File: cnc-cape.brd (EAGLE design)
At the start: 160.7 x 100.3 mm, 120 parts, among them IC1 LM2576hvt, IC2 74HC14N, IC3 74HC14N, IC4 74HCT244N, IC5 74HCT244N, IC6 74HC14N, IC7 LM1458N, J1 22-27-2041-04, J10 22-27-2031-03, J11 22-27-2031-03, J12 22-27-2031-03, J13 22-27-2031-03, J14 22-27-2031-03, J15 22-27-2031-03, J16 22-27-2031-03, J17 22-27-2031-03, J18 22-27-2031-03, J19 22-27-2031-03, J2 22-27-2041-04, J20 22-27-2031-03, J21 22-27-2031-03, J22 22-27-2031-03, J3 22-27-2041-04, J4 22-27-2041-04, J5 22-27-2041-04, J6 22-27-2031-03, J7 22-27-2031-03, J8 22-27-2031-03, J9 22-27-2031-03, K1 G2R2, K2 G2R2, K3 G2R2, Q1 2N7000, Q2 2N7000, T1 1n2222, T2 1n2222, T3 1n2222, X5 Power In

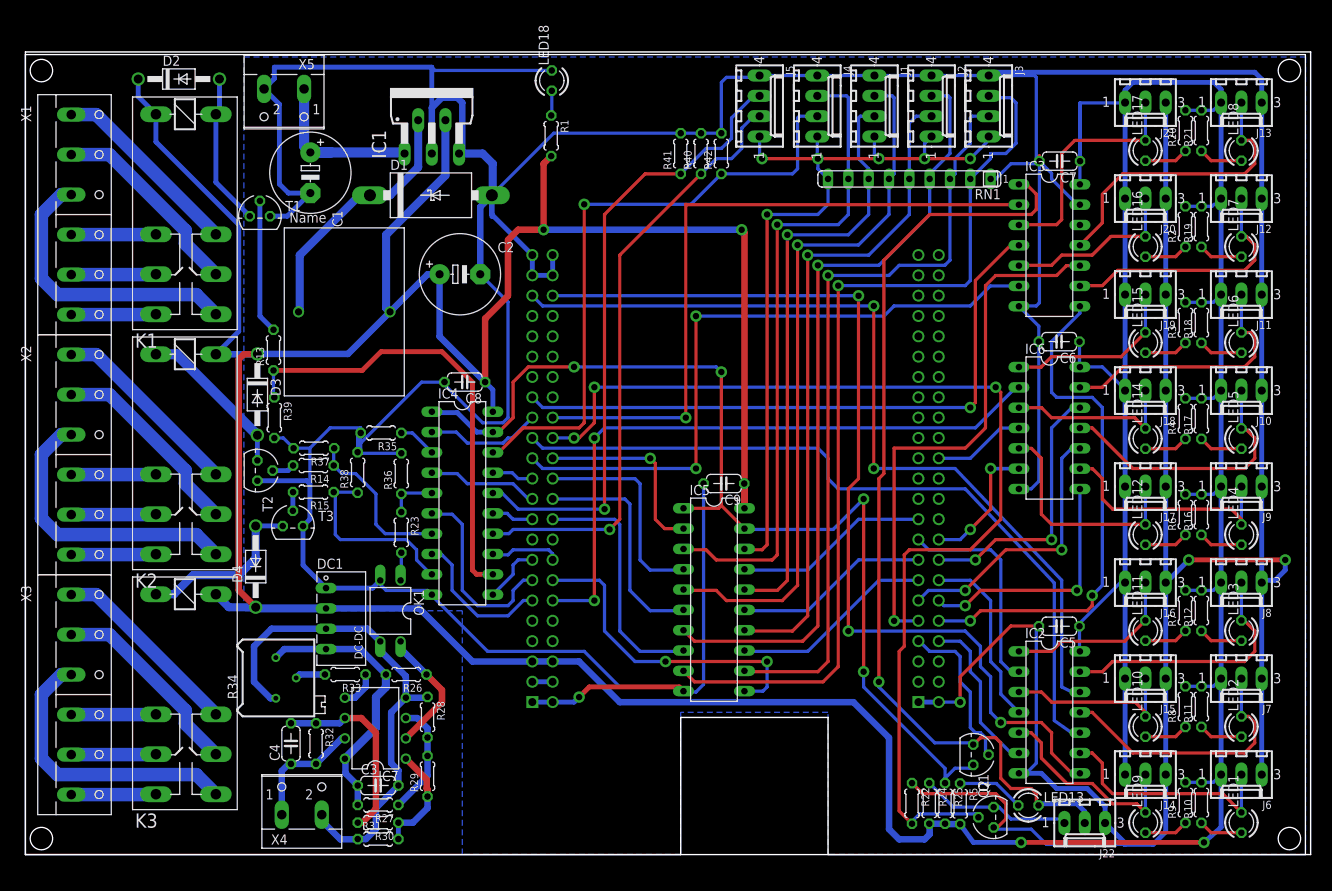
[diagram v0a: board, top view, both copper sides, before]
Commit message: Rearraged layout to reduce via count
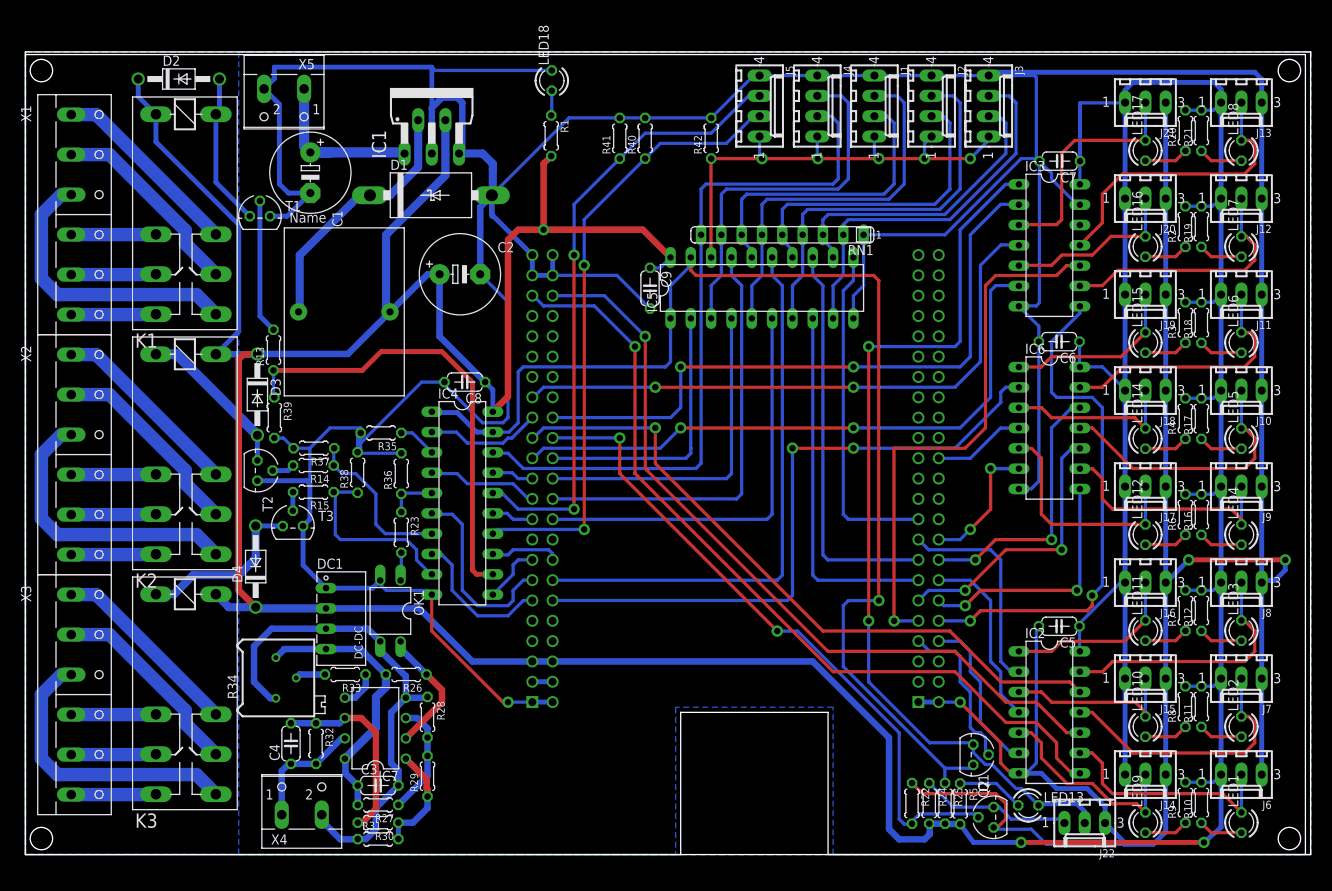
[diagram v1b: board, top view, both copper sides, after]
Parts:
- moved IC5 39.4 mm to (92.1, 70.8), turned to 0 degrees
- moved C9 26.1 mm to (78.1, 70.8), turned to 270 degrees
- moved RN1 17.3 mm to (94.6, 77.5)
- moved R41 7.85 mm to (74.3, 89.5)
- moved R40 7.24 mm to (77.5, 89.5)
- moved R42 2.29 mm to (85.7, 89.5)
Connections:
- net B_DIR_3V renamed P924
- net B_STEP_3V renamed P926
- removed net A_STEP_3V: IC5.6, U$1.68
- removed net PWM0_3V: IC5.8, U$1.66
- removed net PWM1A_3V: IC5.11, U$1.60
- removed net PWM2A_3V: IC5.17, U$1.19
- removed net PWM2B_3V: IC5.13, U$1.13
- removed net X_STEP_3V: IC5.15, U$1.15
- new net P813: IC5.8, U$1.13
- new net P815: IC5.13, U$1.15
- new net P819: IC5.11, U$1.19
- new net P914: IC5.15, U$1.60
- new net P920: IC5.6, U$1.66
- new net P922: IC5.17, U$1.68
- net A_DIR_5V: now also RN1.9; no longer R42.1
- net ENABLE_5V: now also R42.1; no longer RN1.9
- net ENCODER0_A: now also IC2.11, J7.2, LED2.K; no longer IC2.9, J6.2, LED1.K
- net ENCODER0_B: now also IC2.13, J8.2, LED3.K; no longer IC2.11, J7.2, LED2.K
- net ENCODER0_I: now also IC2.9, J6.2, LED1.K; no longer IC2.13, J8.2, LED3.K
- net EQEP0A: now also IC2.10; no longer IC2.8
- net EQEP0B: now also IC2.12; no longer IC2.10
- net EQEP0I: now also IC2.8; no longer IC2.12
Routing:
- net P914: track 0.00 -> 69.2 mm
- net Z_STEP_5V: track 114.6 -> 47.6 mm, vias 1 -> 0
- net Z_DIR_5V: track 96.5 -> 37.8 mm, vias 1 -> 0
- net P922: track 0.00 -> 54.0 mm
- net P920: track 0.00 -> 52.2 mm
- net ESTOP_OUT_3V: track 135.0 -> 83.0 mm, vias 3 -> 2
- net P815: track 0.00 -> 49.9 mm
- net Y_STEP_5V: track 97.9 -> 49.2 mm, vias 1 -> 0
- net P813: track 0.00 -> 45.6 mm
- net Y_DIR_5V: track 83.2 -> 39.5 mm, vias 1 -> 0
- net P819: track 0.00 -> 42.3 mm
- net X_STEP_5V: track 88.6 -> 47.9 mm, vias 1 -> 0
- net PWM1A_3V: track 40.6 -> 0.00 mm, vias 2 -> 0
- net ENABLE_5V: track 100.4 -> 60.3 mm, vias 6 -> 5
- net VDD_5V: track 683.5 -> 644.4 mm, vias 4 -> 3
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- added copper zone on layer 16, net _FILL_
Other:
- outline, holes or cut-outs redrawn
- board text added: "01-16"
- board text added: "01-20"
- board text added: "LAYER-STACK"

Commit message: Fixed pwm polarity
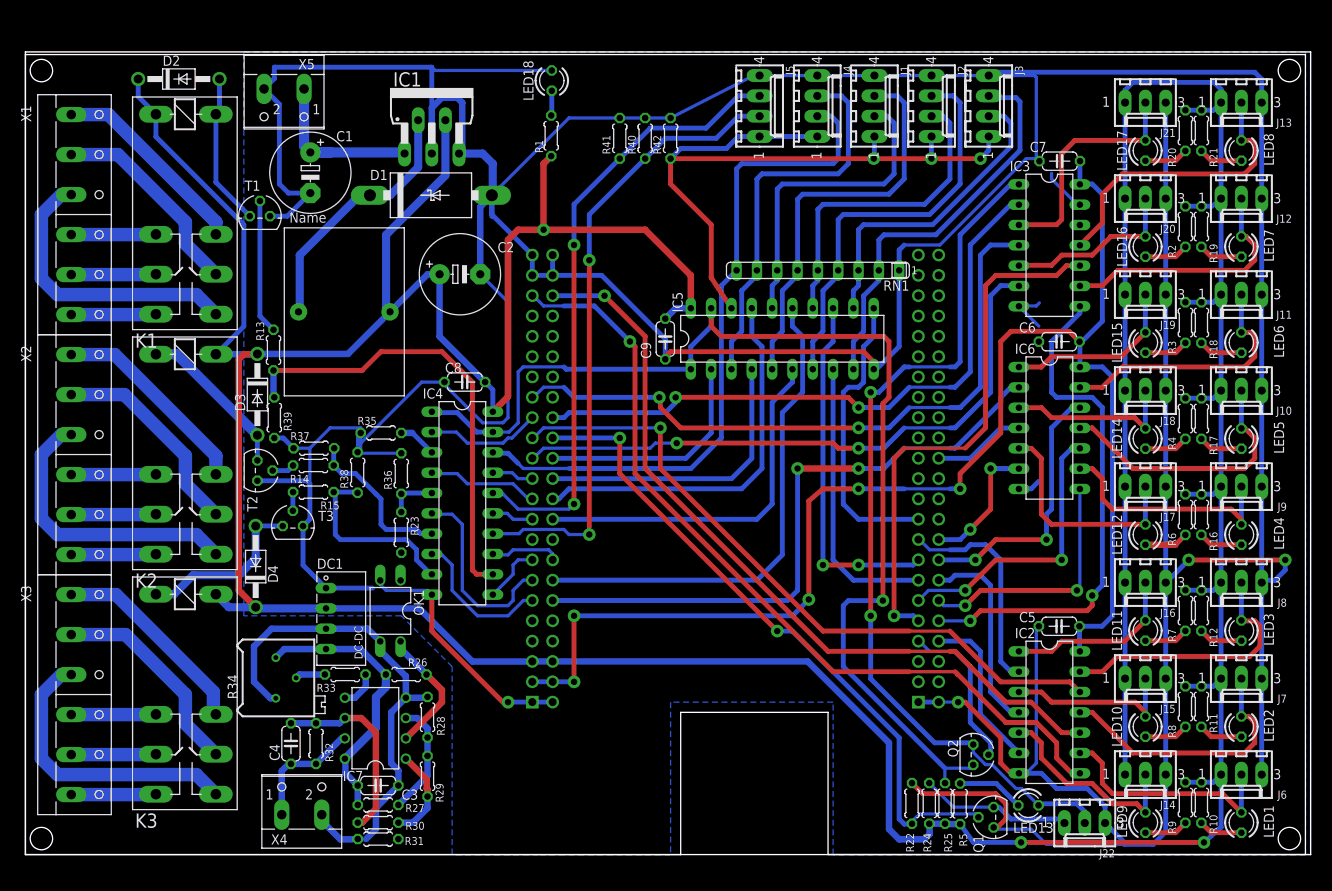
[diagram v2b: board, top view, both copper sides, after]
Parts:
- R38: value k47 -> 4k7
- moved IC5 6.84 mm to (94.6, 64.5)
- moved C9 6.63 mm to (80.0, 64.5)
- moved RN1 6.29 mm to (99.1, 73.0)
- moved R42 5.08 mm to (80.6, 89.5)
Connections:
- net GND: no longer OK1.2
- net N$14: now also R31.2
- net N$45: now also OK1.2; no longer OK1.1
- net N$49: now also R31.1; no longer R31.2
- net SPINDLE-: no longer R31.1
- net VDD_3V3EXP: now also C5.1, C6.1, C7.1, IC2.14, IC3.14, IC6.14
- net VDD_5V: now also OK1.1; no longer C5.1, C6.1, C7.1, IC2.14, IC3.14, IC6.14
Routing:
- net VDD_3V3EXP: track 2.54 -> 178.5 mm, vias 0 -> 5
- net VDD_5V: track 644.4 -> 608.5 mm
- net ENABLE_5V: track 60.3 -> 88.6 mm, vias 5 -> 3
- net !OUTPUT_ENABLE!: track 153.9 -> 143.7 mm
- net P813: track 45.6 -> 35.6 mm
- net SW4_3V: track 75.8 -> 83.3 mm
- net P914: track 69.2 -> 62.4 mm
- net GND: track 780.3 -> 773.8 mm
- net P920: track 52.2 -> 46.1 mm
- net P922: track 54.0 -> 48.3 mm
- net P926: track 34.4 -> 29.1 mm
- net P819: track 42.3 -> 37.0 mm
- net P815: track 49.9 -> 44.8 mm, vias 0 -> 2
- net P924: track 42.0 -> 37.1 mm
- net N$45: track 3.50 -> 0.00 mm
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- removed copper zone on layer 16, net _FILL_

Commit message: Added opto coupled inhibit out put, to disable spindle driver
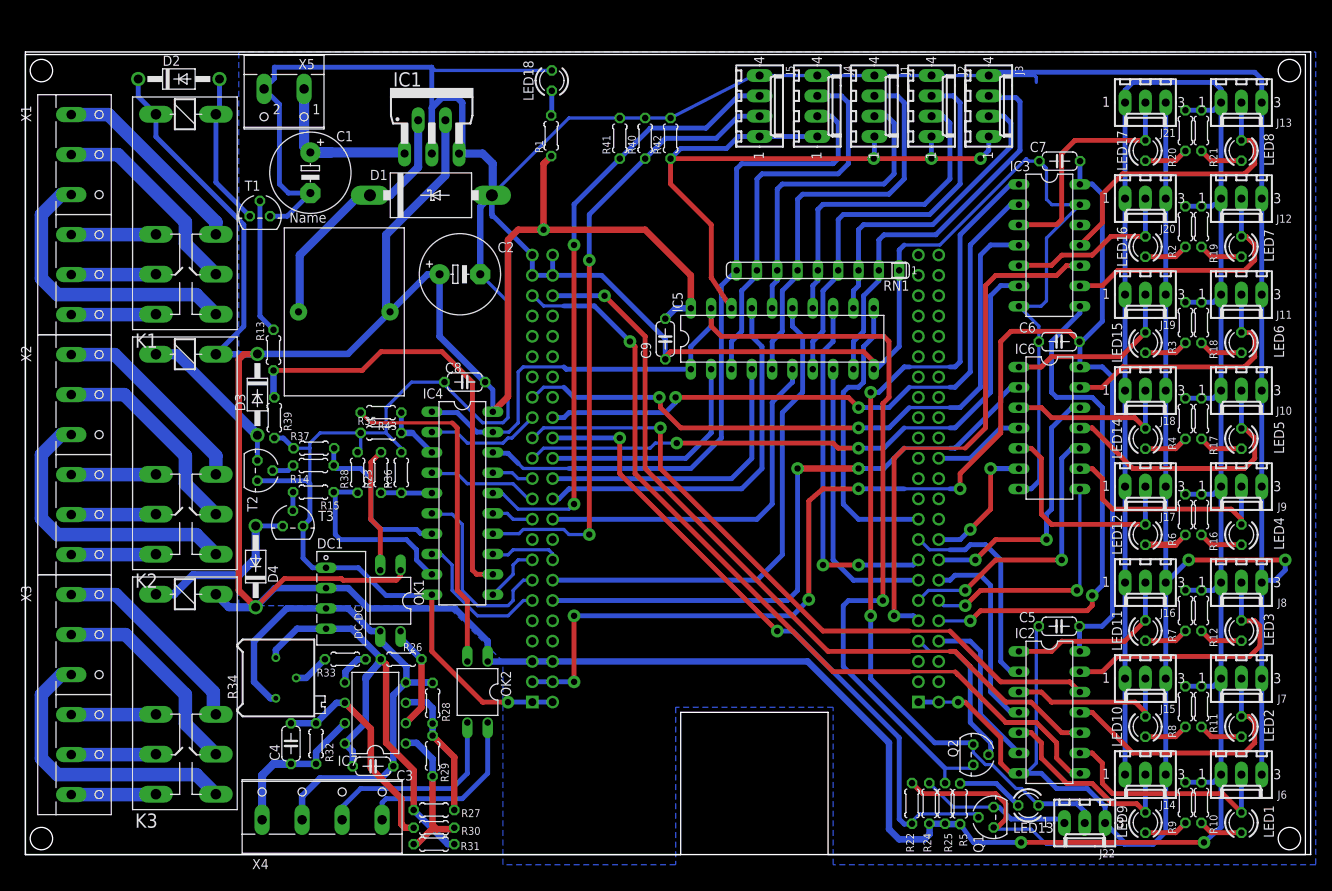
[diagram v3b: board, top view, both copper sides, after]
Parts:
- added OK2: LTV816, optocoupler:DIL04
- added R43: 1k, rcl:0204/5
- X4: device con-wago-500:W237-102 -> con-wago-500:W237-4
- moved R23 7.90 mm to (44.5, 47.8), turned to 90 degrees
- moved R27 7.01 mm to (51.1, 5.57)
- moved R30 7.01 mm to (51.1, 3.35)
- moved R31 7.01 mm to (51.1, 1.30)
- moved R29 2.62 mm to (50.9, 12.3)
- moved X4 2.62 mm to (37.1, 5.62)
- moved DC1 2.54 mm to (37.6, 32.0)
- moved C3 2.49 mm to (43.5, 11.0)
- moved R26 2.01 mm to (47.0, 24.4)
- moved IC7 1.90 mm to (43.7, 17.7)
- moved R33 1.90 mm to (40.0, 24.4)
- moved R28 1.86 mm to (50.9, 18.9)
- moved OK1 1.27 mm to (45.6, 31.7)
- moved R36 0.13 mm to (47.0, 47.8)
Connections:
- removed net RELAY5_5V: IC4.3, R35.1
- new net INHIBIT: IC4.3, R35.1, R43.1
- new net N$46: OK2.4, X4.4
- new net N$51: OK2.3, X4.3
- new net N$52: OK2.2, R43.2
- net VDD_5V: now also OK2.1
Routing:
- net N$52: track 0.00 -> 42.6 mm
- net N$14: track 34.6 -> 63.0 mm
- net GND: track 773.8 -> 800.0 mm
- net N$51: track 0.00 -> 25.3 mm
- net N$46: track 0.00 -> 23.2 mm
- net N$45: track 0.00 -> 15.8 mm
- net VDD_5V: track 608.5 -> 622.8 mm
- net N$49: track 11.7 -> 19.1 mm
- net INHIBIT: track 0.00 -> 7.37 mm
- net RELAY5_5V: track 4.83 -> 0.00 mm
- net SPINDLE+: track 15.0 -> 19.5 mm
- net N$50: track 24.2 -> 27.6 mm
- net N$48: track 14.3 -> 17.6 mm
- net N$47: track 16.1 -> 13.4 mm
- net SPINDLE-: track 63.2 -> 65.5 mm
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
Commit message: fixed some net names
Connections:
- net IN_X_MAX renamed P809
- net IN_X_MIN renamed P810
- net IN_Y_MAX renamed P814
- net IN_Y_MIN renamed P808
- net IN_Z_MAX renamed P818
- net IN_Z_MIN renamed P817
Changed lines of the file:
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@@
 <wire x1="139.995" y1="41.275" x2="140" y2="41.27" width="0.4064" layer="1"/>
 </signal>
-<signal name="IN_X_MIN">
+<signal name="P810">
 <contactref element="IC3" pad="8"/>
 <contactref element="U$1" pad="10"/>
@@
 <wire x1="114.1775" y1="29.21" x2="114.165" y2="29.2225" width="0.4064" layer="16"/>
 </signal>
-<signal name="IN_X_MAX">
+<signal name="P809">
 <contactref element="IC3" pad="10"/>
 <contactref element="U$1" pad="9"/>
@@
 <wire x1="109.855" y1="50.8" x2="117.475" y2="50.8" width="0.4064" layer="1"/>
 </signal>
-<signal name="IN_Y_MIN">
+<signal name="P808">
 <contactref element="IC2" pad="6"/>
 <contactref element="U$1" pad="8"/>
@@
 <wire x1="119.38" y1="17.51" x2="124.19" y2="12.7" width="0.6096" layer="16"/>
 </signal>
-<signal name="IN_Y_MAX">
+<signal name="P814">
 <contactref element="IC2" pad="4"/>
 <contactref element="U$1" pad="14"/>
@@
 <wire x1="123.19" y1="17.78" x2="124.19" y2="17.78" width="0.6096" layer="16"/>
 </signal>
-<signal name="IN_Z_MIN">
+<signal name="P817">
 <contactref element="IC2" pad="2"/>
 <contactref element="U$1" pad="17"/>
@@
 <wire x1="123.19" y1="22.86" x2="124.19" y2="22.86" width="0.6096" layer="16"/>
 </signal>
-<signal name="IN_Z_MAX">
+<signal name="P818">
 <contactref element="IC6" pad="6"/>
 <contactref element="U$1" pad="18"/>
